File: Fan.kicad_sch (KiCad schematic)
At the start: 5 parts, among them J10 Conn_01x02, Q6 AO3400A

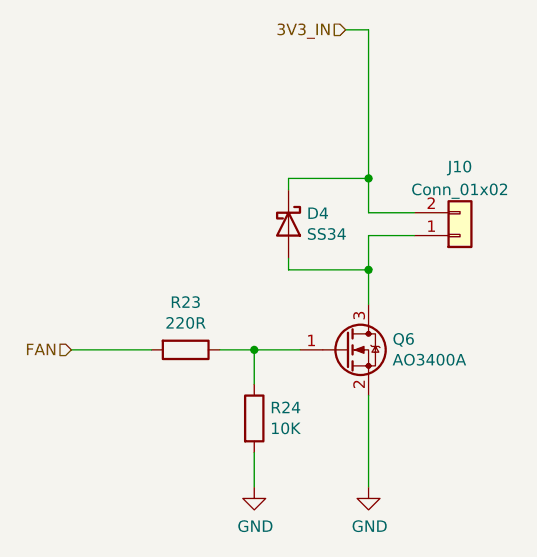
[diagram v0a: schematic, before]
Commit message: Finish component placement
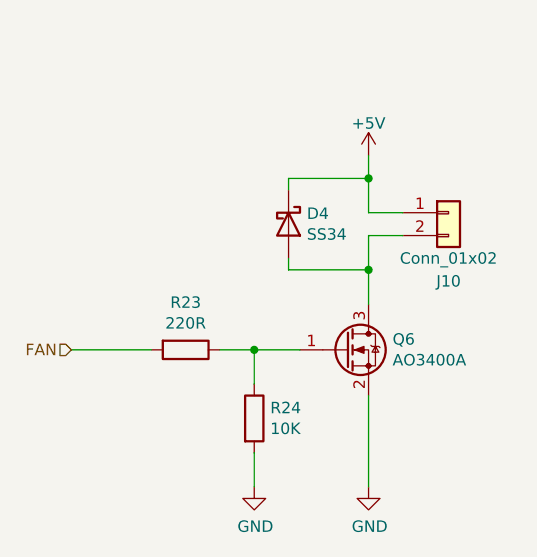
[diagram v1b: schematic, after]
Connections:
- net at D4.2 (A), Q6.3 (D): now also J10.2 (Pin_2); no longer J10.1 (Pin_1)
- net 3V3_IN renamed +5V
- net +5V: now also J10.1 (Pin_1); no longer J10.2 (Pin_2)
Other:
- moved on the sheet: J10
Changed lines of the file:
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@@
-    (stroke (width 0) (type default) (color 0 0 0 0))
-  )
-  (wire (pts (xy 165.1 81.28) (xy 170.18 81.28))
     (stroke (width 0) (type default) (color 0 0 0 0))
   )
@@
     (stroke (width 0) (type default) (color 0 0 0 0))
   )
-  (wire (pts (xy 162.56 58.42) (xy 165.1 58.42))
-    (stroke (width 0) (type default) (color 0 0 0 0))
-  )
   (wire (pts (xy 152.4 97.79) (xy 152.4 93.98))
     (stroke (width 0) (type default) (color 0 0 0 0))
   )
-  (wire (pts (xy 165.1 58.42) (xy 165.1 74.93))
+  (wire (pts (xy 165.1 72.39) (xy 165.1 74.93))
     (stroke (width 0) (type default) (color 0 0 0 0))
   )
-  (wire (pts (xy 170.18 78.74) (xy 165.1 78.74))
+  (wire (pts (xy 165.1 81.28) (xy 168.91 81.28))
     (stroke (width 0) (type default) (color 0 0 0 0))
   )
   (wire (pts (xy 156.21 85.09) (xy 165.1 85.09))
+    (stroke (width 0) (type default) (color 0 0 0 0))
+  )
+  (wire (pts (xy 165.1 78.74) (xy 168.91 78.74))
     (stroke (width 0) (type default) (color 0 0 0 0))
   )
@@
   (wire (pts (xy 165.1 78.74) (xy 165.1 74.93))
     (stroke (width 0) (type default) (color 0 0 0 0))
-  )
-  (hierarchical_label "3V3_IN" (shape input) (at 162.56 58.42 180)
-    (effects (font (size 1.27 1.27)) (justify right))
   )
   (hierarchical_label "FAN" (shape input) (at 132.08 93.98 180)
@@
     (pin "2")
   )
-  (symbol (lib_id "Connector_Generic:Conn_01x02") (at 175.26 81.28 0) (mirror x) (unit 1)
+  (symbol (lib_id "Connector_Generic:Conn_01x02") (at 173.99 78.74 0) (unit 1)
     (in_bom yes) (on_board yes)
-    (property "Reference" "J10" (id 0) (at 175.26 73.66 0))
-    (property "Value" "Conn_01x02" (id 1) (at 175.26 76.2 0))
-    (property "Footprint" "Connector_JST:JST_XH_B2B-XH-AM_1x02_P2.50mm_Vertical" (id 2) (at 175.26 81.28 0)
+    (property "Reference" "J10" (id 0) (at 173.99 86.36 0))
+    (property "Value" "Conn_01x02" (id 1) (at 173.99 83.82 0))
+    (property "Footprint" "Connector_JST:JST_XH_B2B-XH-AM_1x02_P2.50mm_Vertical" (id 2) (at 173.99 78.74 0)
       (effects (font (size 1.27 1.27)) hide)
     )
-    (property "Datasheet" "~" (id 3) (at 175.26 81.28 0)
+    (property "Datasheet" "~" (id 3) (at 173.99 78.74 0)
       (effects (font (size 1.27 1.27)) hide)
     )
-    (property "LCSC" "C20079" (id 4) (at 175.26 81.28 0)
+    (property "LCSC" "C20079" (id 4) (at 173.99 78.74 0)
       (effects (font (size 1.27 1.27)) hide)
     )
@@
     (pin "2")
   )
+  (symbol (lib_id "power:+5V") (at 165.1 72.39 0) (unit 1)
+    (in_bom yes) (on_board yes) (fields_autoplaced)
+    (property "Reference" "#PWR0101" (id 0) (at 165.1 76.2 0)
+      (effects (font (size 1.27 1.27)) hide)
+    )
+    (property "Value" "+5V" (id 1) (at 165.1 68.8142 0))
+    (property "Footprint" "" (id 2) (at 165.1 72.39 0)
+      (effects (font (size 1.27 1.27)) hide)
+    )
+    (property "Datasheet" "" (id 3) (at 165.1 72.39 0)
+      (effects (font (size 1.27 1.27)) hide)
+    )
+    (pin "1")
+  )
 )

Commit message: I was never here
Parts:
- renumbered R23 to R24, R24 to R25
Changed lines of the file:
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@@
   (symbol (lib_id "Device:R") (at 144.78 93.98 270) (unit 1)
     (in_bom yes) (on_board yes)
-    (property "Reference" "R23" (id 0) (at 144.78 88.7222 90))
+    (property "Reference" "R24" (id 0) (at 144.78 88.7222 90))
     (property "Value" "220R" (id 1) (at 144.78 91.0336 90))
     (property "Footprint" "Resistor_SMD:R_0603_1608Metric" (id 2) (at 144.78 92.202 90)
@@
   (symbol (lib_id "Device:R") (at 152.4 101.6 0) (unit 1)
     (in_bom yes) (on_board yes)
-    (property "Reference" "R24" (id 0) (at 154.178 100.4316 0)
+    (property "Reference" "R25" (id 0) (at 154.178 100.4316 0)
       (effects (font (size 1.27 1.27)) (justify left))
     )
@@
   (symbol (lib_id "power:GND") (at 152.4 109.22 0) (unit 1)
     (in_bom yes) (on_board yes)
-    (property "Reference" "#PWR060" (id 0) (at 152.4 115.57 0)
+    (property "Reference" "#PWR061" (id 0) (at 152.4 115.57 0)
       (effects (font (size 1.27 1.27)) hide)
     )
@@
   (symbol (lib_id "power:GND") (at 165.1 109.22 0) (unit 1)
     (in_bom yes) (on_board yes)
-    (property "Reference" "#PWR061" (id 0) (at 165.1 115.57 0)
+    (property "Reference" "#PWR063" (id 0) (at 165.1 115.57 0)
       (effects (font (size 1.27 1.27)) hide)
     )
@@
   (symbol (lib_id "power:+5V") (at 165.1 72.39 0) (unit 1)
     (in_bom yes) (on_board yes) (fields_autoplaced)
-    (property "Reference" "#PWR0101" (id 0) (at 165.1 76.2 0)
+    (property "Reference" "#PWR062" (id 0) (at 165.1 76.2 0)
       (effects (font (size 1.27 1.27)) hide)
     )

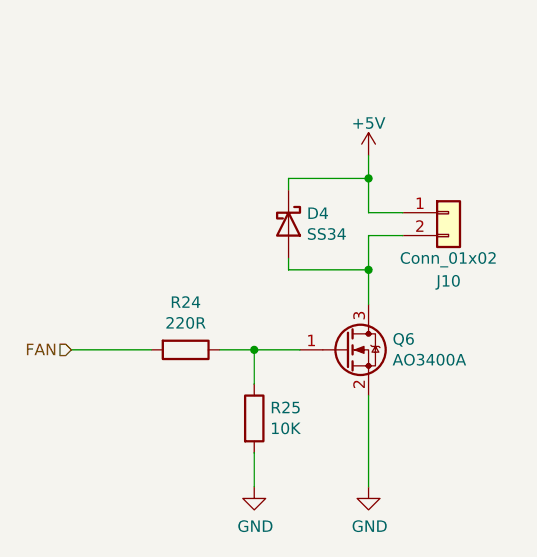
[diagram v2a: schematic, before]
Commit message: Finish routing round 2
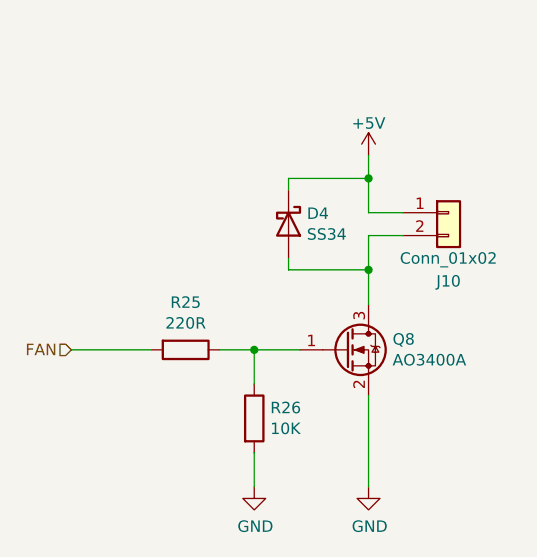
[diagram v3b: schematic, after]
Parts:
- renumbered Q6 to Q8, R24 to R25, R25 to R26
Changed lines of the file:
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@@
   (symbol (lib_id "Transistor_FET:AO3400A") (at 162.56 93.98 0) (unit 1)
     (in_bom yes) (on_board yes)
-    (property "Reference" "Q6" (id 0) (at 167.767 92.8116 0)
+    (property "Reference" "Q8" (id 0) (at 167.767 92.8116 0)
       (effects (font (size 1.27 1.27)) (justify left))
     )
@@
   (symbol (lib_id "Device:R") (at 144.78 93.98 270) (unit 1)
     (in_bom yes) (on_board yes)
-    (property "Reference" "R24" (id 0) (at 144.78 88.7222 90))
+    (property "Reference" "R25" (id 0) (at 144.78 88.7222 90))
     (property "Value" "220R" (id 1) (at 144.78 91.0336 90))
     (property "Footprint" "Resistor_SMD:R_0603_1608Metric" (id 2) (at 144.78 92.202 90)
@@
   (symbol (lib_id "Device:R") (at 152.4 101.6 0) (unit 1)
     (in_bom yes) (on_board yes)
-    (property "Reference" "R25" (id 0) (at 154.178 100.4316 0)
+    (property "Reference" "R26" (id 0) (at 154.178 100.4316 0)
       (effects (font (size 1.27 1.27)) (justify left))
     )
@@
   (symbol (lib_id "power:GND") (at 152.4 109.22 0) (unit 1)
     (in_bom yes) (on_board yes)
-    (property "Reference" "#PWR061" (id 0) (at 152.4 115.57 0)
+    (property "Reference" "#PWR063" (id 0) (at 152.4 115.57 0)
       (effects (font (size 1.27 1.27)) hide)
     )
@@
   (symbol (lib_id "power:GND") (at 165.1 109.22 0) (unit 1)
     (in_bom yes) (on_board yes)
-    (property "Reference" "#PWR063" (id 0) (at 165.1 115.57 0)
+    (property "Reference" "#PWR065" (id 0) (at 165.1 115.57 0)
       (effects (font (size 1.27 1.27)) hide)
     )
@@
   (symbol (lib_id "power:+5V") (at 165.1 72.39 0) (unit 1)
     (in_bom yes) (on_board yes) (fields_autoplaced)
-    (property "Reference" "#PWR062" (id 0) (at 165.1 76.2 0)
+    (property "Reference" "#PWR064" (id 0) (at 165.1 76.2 0)
       (effects (font (size 1.27 1.27)) hide)
     )
